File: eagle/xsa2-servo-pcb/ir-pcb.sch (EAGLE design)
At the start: 36 parts, among them IC1 ATMEGA328P-AU, IC2 PL-IRM0101, IC3 PL-IRM0101, IC4 PL-IRM0101, IC5 PL-IRM0101, IC6 PL-IRM0101, IC7 PL-IRM0101, Q1 IRLML6402, Q2 IRFML8244, Q3 IRFML8244, Q4 IRFML8244, Q5 8MHz

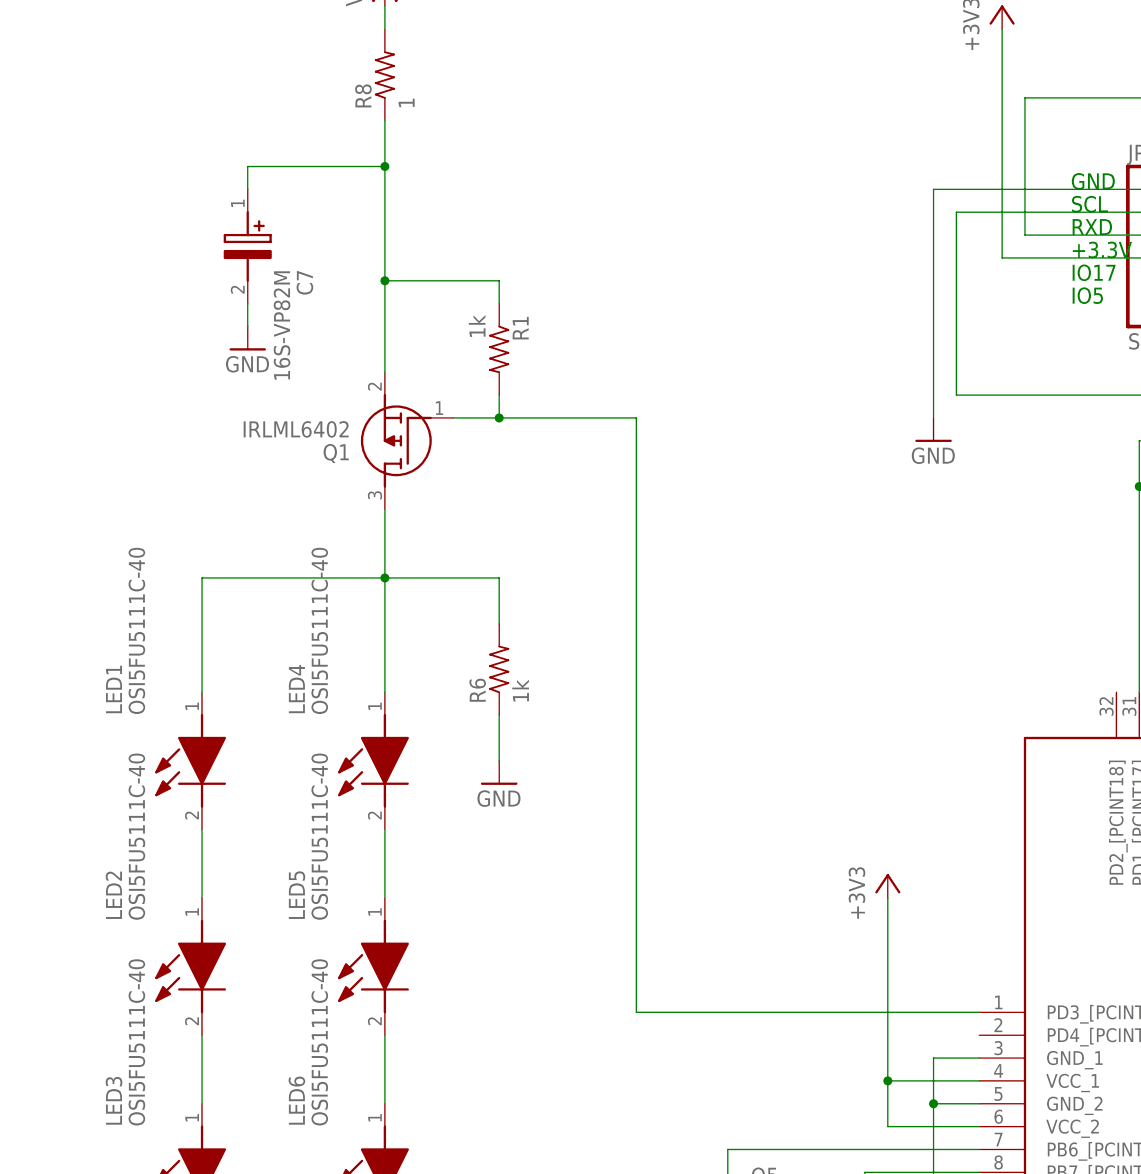
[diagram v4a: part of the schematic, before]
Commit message: [eagle] 赤外発光部のPMOSにNMOSを追加
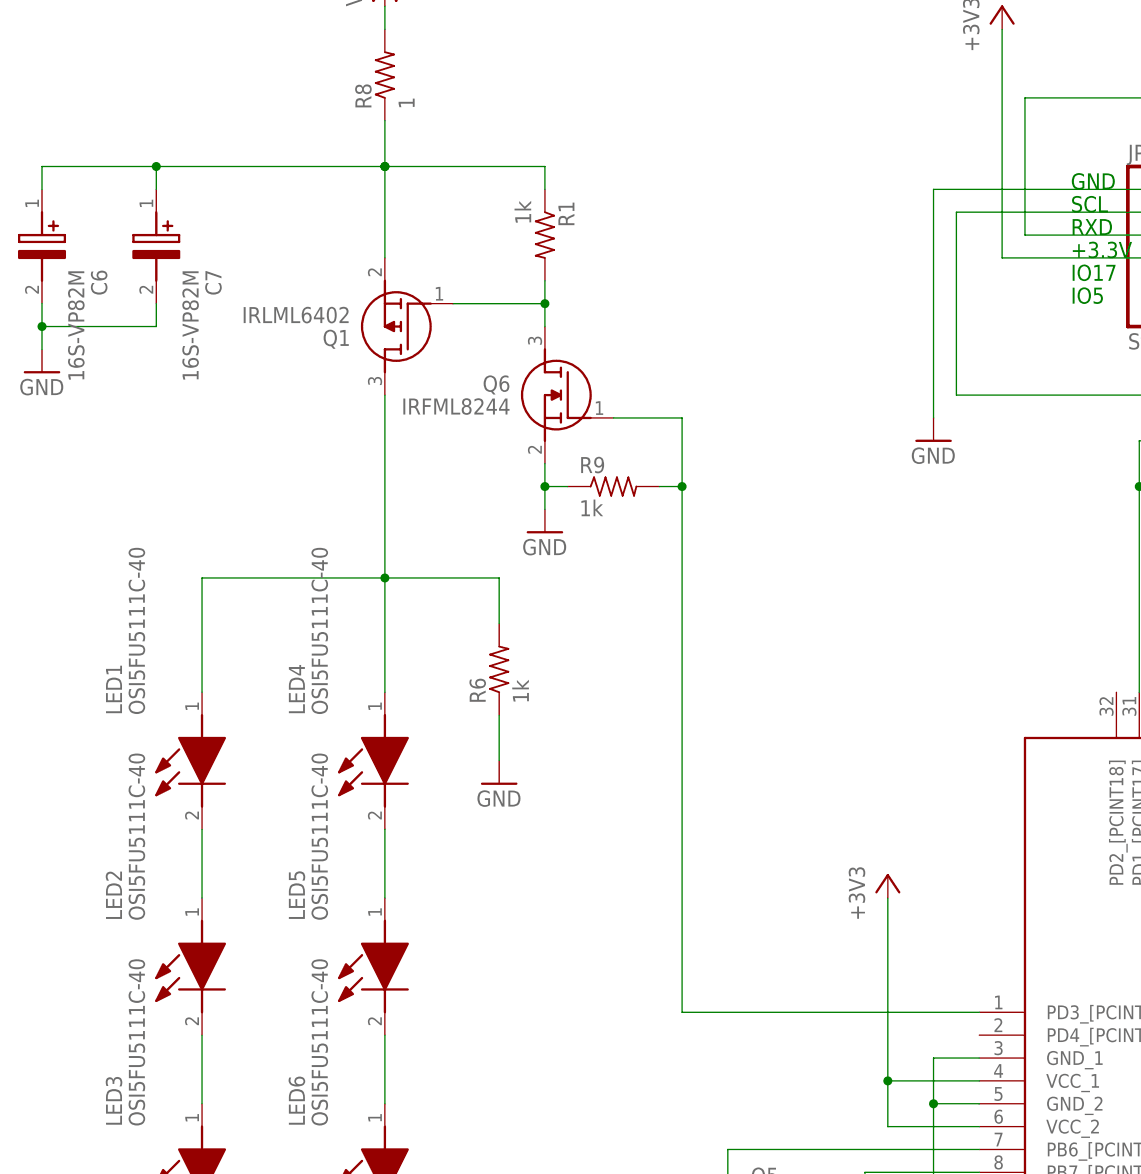
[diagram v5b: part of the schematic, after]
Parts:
- added C6: 16S-VP82M, SamacSys_Parts:16S-VP82M
- added Q6: IRFML8244, SamacSys_Parts:IRFML8244
- added R9: 1k, rcl:R-US_R0603
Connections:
- new net N$2: Q1.G, Q6.D, R1.2
- net GND: now also C6.-, Q6.S, R9.1
- net N$10: now also Q6.G, R9.2; no longer Q1.G, R1.2
- net N$27: now also C6.+
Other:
- moved on the sheet: C7, Q1, R1
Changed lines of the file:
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@@
 <part name="C7" library="SamacSys_Parts" deviceset="16S-VP82M" device=""/>
 <part name="FRAME1" library="frames" library_urn="urn:adsk.eagle:library:229" deviceset="A3L-LOC" device=""/>
+<part name="Q6" library="SamacSys_Parts" deviceset="IRFML8244" device=""/>
+<part name="GND11" library="supply1" library_urn="urn:adsk.eagle:library:371" deviceset="GND" device=""/>
+<part name="R9" library="rcl" library_urn="urn:adsk.eagle:library:334" deviceset="R-US_" device="R0603" package3d_urn="urn:adsk.eagle:package:23555/3" value="1k"/>
+<part name="C6" library="SamacSys_Parts" deviceset="16S-VP82M" device=""/>
 </parts>
 <sheets>
@@
 <attribute name="VALUE" x="58.42" y="-124.46" size="1.778" layer="96"/>
 </instance>
-<instance part="R1" gate="G$1" x="-81.28" y="78.74" smashed="yes" rot="R270">
-<attribute name="NAME" x="-79.7814" y="82.55" size="1.778" layer="95" rot="R270"/>
-<attribute name="VALUE" x="-84.582" y="82.55" size="1.778" layer="96" rot="R270"/>
+<instance part="R1" gate="G$1" x="-76.2" y="91.44" smashed="yes" rot="R270">
+<attribute name="NAME" x="-74.7014" y="95.25" size="1.778" layer="95" rot="R270"/>
+<attribute name="VALUE" x="-79.502" y="95.25" size="1.778" layer="96" rot="R270"/>
 </instance>
 <instance part="R2" gate="G$1" x="-121.92" y="-33.02" smashed="yes" rot="R90">
@@
 <attribute name="VALUE" x="-76.2" y="-101.6" size="1.778" layer="96"/>
 </instance>
-<instance part="Q1" gate="G$1" x="-86.36" y="71.12" smashed="yes" rot="R180">
-<attribute name="NAME" x="-97.79" y="67.31" size="1.778" layer="95" rot="R180" align="center-left"/>
-<attribute name="VALUE" x="-97.79" y="69.85" size="1.778" layer="96" rot="R180" align="center-left"/>
+<instance part="Q1" gate="G$1" x="-86.36" y="83.82" smashed="yes" rot="R180">
+<attribute name="NAME" x="-97.79" y="80.01" size="1.778" layer="95" rot="R180" align="center-left"/>
+<attribute name="VALUE" x="-97.79" y="82.55" size="1.778" layer="96" rot="R180" align="center-left"/>
 </instance>
 <instance part="Q2" gate="G$1" x="-106.68" y="-53.34" smashed="yes" rot="MR0">
@@
 <attribute name="VALUE" x="-90.678" y="105.41" size="1.778" layer="96" rot="R90"/>
 </instance>
-<instance part="GND10" gate="1" x="-109.22" y="78.74" smashed="yes">
-<attribute name="VALUE" x="-111.76" y="76.2" size="1.778" layer="96"/>
-</instance>
-<instance part="C7" gate="G$1" x="-109.22" y="96.52" smashed="yes" rot="R270">
-<attribute name="NAME" x="-102.87" y="87.63" size="1.778" layer="95" rot="R270" align="center-left"/>
-<attribute name="VALUE" x="-105.41" y="87.63" size="1.778" layer="96" rot="R270" align="center-left"/>
+<instance part="GND10" gate="1" x="-132.08" y="76.2" smashed="yes">
+<attribute name="VALUE" x="-134.62" y="73.66" size="1.778" layer="96"/>
+</instance>
+<instance part="C7" gate="G$1" x="-119.38" y="96.52" smashed="yes" rot="R270">
+<attribute name="NAME" x="-113.03" y="87.63" size="1.778" layer="95" rot="R270" align="center-left"/>
+<attribute name="VALUE" x="-115.57" y="87.63" size="1.778" layer="96" rot="R270" align="center-left"/>
 </instance>
 <instance part="FRAME1" gate="G$1" x="-198.12" y="-132.08" smashed="yes">
@@
 <attribute name="LAST_DATE_TIME" x="146.05" y="-121.92" size="2.286" layer="94"/>
 <attribute name="SHEET" x="159.385" y="-127" size="2.54" layer="94"/>
+</instance>
+<instance part="Q6" gate="G$1" x="-68.58" y="71.12" smashed="yes" rot="MR0">
+<attribute name="NAME" x="-80.01" y="74.93" size="1.778" layer="95" rot="MR0" align="center-left"/>
+<attribute name="VALUE" x="-80.01" y="72.39" size="1.778" layer="96" rot="MR0" align="center-left"/>
+</instance>
+<instance part="GND11" gate="1" x="-76.2" y="58.42" smashed="yes">
+<attribute name="VALUE" x="-78.74" y="55.88" size="1.778" layer="96"/>
+</instance>
+<instance part="R9" gate="G$1" x="-68.58" y="63.5" smashed="yes">
+<attribute name="NAME" x="-72.39" y="64.9986" size="1.778" layer="95"/>
+<attribute name="VALUE" x="-72.39" y="60.198" size="1.778" layer="96"/>
+</instance>
+<instance part="C6" gate="G$1" x="-132.08" y="96.52" smashed="yes" rot="R270">
+<attribute name="NAME" x="-125.73" y="87.63" size="1.778" layer="95" rot="R270" align="center-left"/>
+<attribute name="VALUE" x="-128.27" y="87.63" size="1.778" layer="96" rot="R270" align="center-left"/>
 </instance>
 </instances>
@@
 <pinref part="C7" gate="G$1" pin="-"/>
 <pinref part="GND10" gate="1" pin="GND"/>
-<wire x1="-109.22" y1="83.82" x2="-109.22" y2="81.28" width="0.1524" layer="91"/>
+<wire x1="-119.38" y1="83.82" x2="-119.38" y2="81.28" width="0.1524" layer="91"/>
+<wire x1="-119.38" y1="81.28" x2="-132.08" y2="81.28" width="0.1524" layer="91"/>
+<wire x1="-132.08" y1="81.28" x2="-132.08" y2="78.74" width="0.1524" layer="91"/>
+<pinref part="C6" gate="G$1" pin="-"/>
+<wire x1="-132.08" y1="81.28" x2="-132.08" y2="83.82" width="0.1524" layer="91"/>
+<junction x="-132.08" y="81.28"/>
+</segment>
+<segment>
+<pinref part="Q6" gate="G$1" pin="S"/>
+<pinref part="GND11" gate="1" pin="GND"/>
+<wire x1="-76.2" y1="66.04" x2="-76.2" y2="63.5" width="0.1524" layer="91"/>
+<pinref part="R9" gate="G$1" pin="1"/>
+<wire x1="-76.2" y1="63.5" x2="-76.2" y2="60.96" width="0.1524" layer="91"/>
+<wire x1="-76.2" y1="63.5" x2="-73.66" y2="63.5" width="0.1524" layer="91"/>
+<junction x="-76.2" y="63.5"/>
 </segment>
 </net>
@@
 <segment>
 <pinref part="IC1" gate="G$1" pin="PD3_[PCINT19]"/>
-<wire x1="-27.94" y1="5.08" x2="-66.04" y2="5.08" width="0.1524" layer="91"/>
-<wire x1="-66.04" y1="5.08" x2="-66.04" y2="71.12" width="0.1524" layer="91"/>
-<wire x1="-66.04" y1="71.12" x2="-81.28" y2="71.12" width="0.1524" layer="91"/>
-<pinref part="R1" gate="G$1" pin="2"/>
-<wire x1="-81.28" y1="71.12" x2="-86.36" y2="71.12" width="0.1524" layer="91"/>
-<wire x1="-81.28" y1="73.66" x2="-81.28" y2="71.12" width="0.1524" layer="91"/>
-<junction x="-81.28" y="71.12"/>
-<pinref part="Q1" gate="G$1" pin="G"/>
+<wire x1="-27.94" y1="5.08" x2="-60.96" y2="5.08" width="0.1524" layer="91"/>
+<pinref part="Q6" gate="G$1" pin="G"/>
+<wire x1="-68.58" y1="71.12" x2="-60.96" y2="71.12" width="0.1524" layer="91"/>
+<wire x1="-60.96" y1="71.12" x2="-60.96" y2="63.5" width="0.1524" layer="91"/>
+<pinref part="R9" gate="G$1" pin="2"/>
+<wire x1="-60.96" y1="63.5" x2="-60.96" y2="5.08" width="0.1524" layer="91"/>
+<wire x1="-63.5" y1="63.5" x2="-60.96" y2="63.5" width="0.1524" layer="91"/>
+<junction x="-60.96" y="63.5"/>
 </segment>
 </net>
@@
 <wire x1="-114.3" y1="53.34" x2="-93.98" y2="53.34" width="0.1524" layer="91"/>
 <wire x1="-93.98" y1="53.34" x2="-93.98" y2="40.64" width="0.1524" layer="91"/>
-<wire x1="-93.98" y1="53.34" x2="-93.98" y2="60.96" width="0.1524" layer="91"/>
+<wire x1="-93.98" y1="53.34" x2="-93.98" y2="73.66" width="0.1524" layer="91"/>
 <junction x="-93.98" y="53.34"/>
 <pinref part="Q1" gate="G$1" pin="D"/>
@@
 <segment>
 <pinref part="R1" gate="G$1" pin="1"/>
-<wire x1="-93.98" y1="86.36" x2="-93.98" y2="76.2" width="0.1524" layer="91"/>
-<wire x1="-81.28" y1="83.82" x2="-81.28" y2="86.36" width="0.1524" layer="91"/>
-<wire x1="-81.28" y1="86.36" x2="-93.98" y2="86.36" width="0.1524" layer="91"/>
-<junction x="-93.98" y="86.36"/>
+<wire x1="-93.98" y1="99.06" x2="-93.98" y2="88.9" width="0.1524" layer="91"/>
+<wire x1="-76.2" y1="96.52" x2="-76.2" y2="99.06" width="0.1524" layer="91"/>
+<wire x1="-76.2" y1="99.06" x2="-93.98" y2="99.06" width="0.1524" layer="91"/>
+<junction x="-93.98" y="99.06"/>
 <pinref part="Q1" gate="G$1" pin="S"/>
 <wire x1="-93.98" y1="104.14" x2="-93.98" y2="99.06" width="0.1524" layer="91"/>
 <pinref part="R8" gate="G$1" pin="1"/>
-<wire x1="-93.98" y1="99.06" x2="-93.98" y2="86.36" width="0.1524" layer="91"/>
-<wire x1="-109.22" y1="96.52" x2="-109.22" y2="99.06" width="0.1524" layer="91"/>
-<wire x1="-109.22" y1="99.06" x2="-93.98" y2="99.06" width="0.1524" layer="91"/>
+<wire x1="-119.38" y1="96.52" x2="-119.38" y2="99.06" width="0.1524" layer="91"/>
+<wire x1="-119.38" y1="99.06" x2="-93.98" y2="99.06" width="0.1524" layer="91"/>
 <junction x="-93.98" y="99.06"/>
 <pinref part="C7" gate="G$1" pin="+"/>
-</segment>
-</net>
+<wire x1="-119.38" y1="99.06" x2="-132.08" y2="99.06" width="0.1524" layer="91"/>
+<junction x="-119.38" y="99.06"/>
+<pinref part="C6" gate="G$1" pin="+"/>
+<wire x1="-132.08" y1="99.06" x2="-132.08" y2="96.52" width="0.1524" layer="91"/>
+</segment>
+</net>
+<net name="N$2" class="0">
+<segment>
+<pinref part="Q1" gate="G$1" pin="G"/>
+<wire x1="-76.2" y1="83.82" x2="-86.36" y2="83.82" width="0.1524" layer="91"/>
+<pinref part="R1" gate="G$1" pin="2"/>
+<wire x1="-76.2" y1="86.36" x2="-76.2" y2="83.82" width="0.1524" layer="91"/>
+<pinref part="Q6" gate="G$1" pin="D"/>
+<wire x1="-76.2" y1="81.28" x2="-76.2" y2="83.82" width="0.1524" layer="91"/>
+<junction x="-76.2" y="83.82"/>
+</segment>
+</net>
